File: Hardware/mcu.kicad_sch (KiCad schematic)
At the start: 10 parts, among them Q1 BSS138DW-7-F, U6 AS7341-DLGT

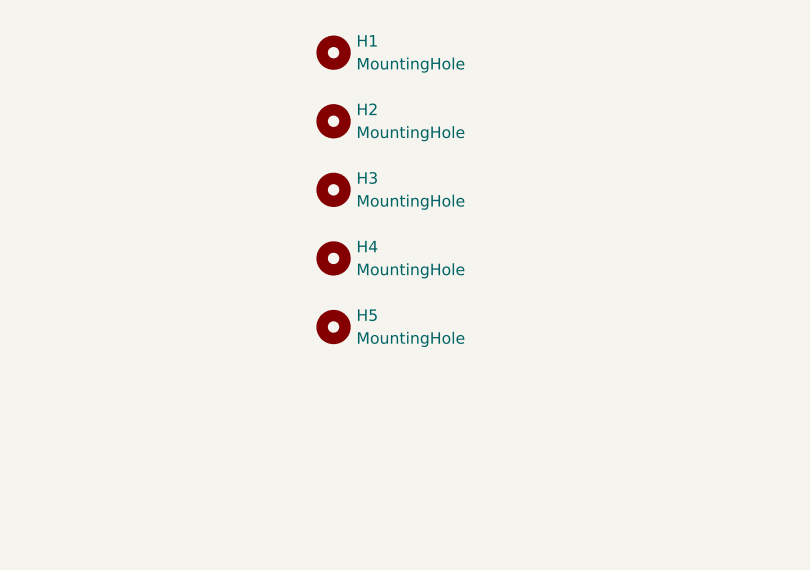
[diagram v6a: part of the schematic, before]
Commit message: initial branch commit with rought layout changes
Signed-off-by: Lawrence Kincheloe <lawrence.kincheloe@mavericktechok.com>
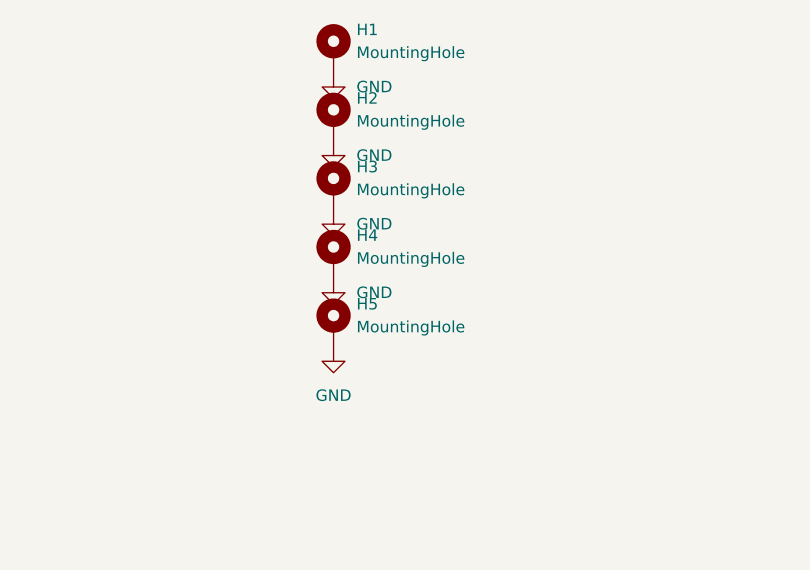
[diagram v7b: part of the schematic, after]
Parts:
- H1, H2, H3, H4, H5: symbol Mechanical:MountingHole -> Mechanical:MountingHole_Pad
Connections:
- net GND: now also H1.1, H2.1, H3.1, H4.1, H5.1
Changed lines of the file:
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@@
     (pin "2")
   )
-  (symbol (lib_id "Mechanical:MountingHole") (at 182.88 39.37 0) (unit 1)
-    (in_bom yes) (on_board yes) (fields_autoplaced)
-    (property "Reference" "H2" (id 0) (at 185.42 38.0999 0)
-      (effects (font (size 1.27 1.27)) (justify left))
-    )
-    (property "Value" "MountingHole" (id 1) (at 185.42 40.6399 0)
+  (symbol (lib_id "power:GND") (at 182.88 64.77 0) (unit 1)
+    (in_bom yes) (on_board yes) (fields_autoplaced)
+    (property "Reference" "#PWR0134" (id 0) (at 182.88 71.12 0)
+      (effects (font (size 1.27 1.27)) hide)
+    )
+    (property "Value" "GND" (id 1) (at 182.88 69.85 0))
+    (property "Footprint" "" (id 2) (at 182.88 64.77 0)
+      (effects (font (size 1.27 1.27)) hide)
+    )
+    (property "Datasheet" "" (id 3) (at 182.88 64.77 0)
+      (effects (font (size 1.27 1.27)) hide)
+    )
+    (pin "1")
+  )
+  (symbol (lib_id "power:GND") (at 182.88 34.29 0) (unit 1)
+    (in_bom yes) (on_board yes) (fields_autoplaced)
+    (property "Reference" "#PWR0112" (id 0) (at 182.88 40.64 0)
+      (effects (font (size 1.27 1.27)) hide)
+    )
+    (property "Value" "GND" (id 1) (at 185.42 35.5599 0)
+      (effects (font (size 1.27 1.27)) (justify left))
+    )
+    (property "Footprint" "" (id 2) (at 182.88 34.29 0)
+      (effects (font (size 1.27 1.27)) hide)
+    )
+    (property "Datasheet" "" (id 3) (at 182.88 34.29 0)
+      (effects (font (size 1.27 1.27)) hide)
+    )
+    (pin "1")
+  )
+  (symbol (lib_id "Mechanical:MountingHole_Pad") (at 182.88 39.37 0) (unit 1)
+    (in_bom yes) (on_board yes) (fields_autoplaced)
+    (property "Reference" "H2" (id 0) (at 185.42 36.8299 0)
+      (effects (font (size 1.27 1.27)) (justify left))
+    )
+    (property "Value" "MountingHole" (id 1) (at 185.42 39.3699 0)
       (effects (font (size 1.27 1.27)) (justify left))
     )
@@
       (effects (font (size 1.27 1.27)) hide)
     )
+    (pin "1")
   )
   (symbol (lib_id "Everlight-EAHC2835WD6:EAHC2835WD6") (at 180.34 102.87 270) (unit 1)
@@
     (pin "2")
   )
-  (symbol (lib_id "Mechanical:MountingHole") (at 182.88 62.23 0) (unit 1)
-    (in_bom yes) (on_board yes) (fields_autoplaced)
-    (property "Reference" "H5" (id 0) (at 185.42 60.9599 0)
-      (effects (font (size 1.27 1.27)) (justify left))
-    )
-    (property "Value" "MountingHole" (id 1) (at 185.42 63.4999 0)
+  (symbol (lib_id "Mechanical:MountingHole_Pad") (at 182.88 62.23 0) (unit 1)
+    (in_bom yes) (on_board yes) (fields_autoplaced)
+    (property "Reference" "H5" (id 0) (at 185.42 59.6899 0)
+      (effects (font (size 1.27 1.27)) (justify left))
+    )
+    (property "Value" "MountingHole" (id 1) (at 185.42 62.2299 0)
       (effects (font (size 1.27 1.27)) (justify left))
     )
@@
       (effects (font (size 1.27 1.27)) hide)
     )
+    (pin "1")
   )
   (symbol (lib_id "power:+3.3V") (at 180.34 102.87 0) (unit 1)
@@
     (pin "1")
   )
-  (symbol (lib_id "Mechanical:MountingHole") (at 182.88 46.99 0) (unit 1)
-    (in_bom yes) (on_board yes) (fields_autoplaced)
-    (property "Reference" "H3" (id 0) (at 185.42 45.7199 0)
-      (effects (font (size 1.27 1.27)) (justify left))
-    )
-    (property "Value" "MountingHole" (id 1) (at 185.42 48.2599 0)
+  (symbol (lib_id "power:GND") (at 182.88 49.53 0) (unit 1)
+    (in_bom yes) (on_board yes) (fields_autoplaced)
+    (property "Reference" "#PWR0135" (id 0) (at 182.88 55.88 0)
+      (effects (font (size 1.27 1.27)) hide)
+    )
+    (property "Value" "GND" (id 1) (at 185.42 50.7999 0)
+      (effects (font (size 1.27 1.27)) (justify left))
+    )
+    (property "Footprint" "" (id 2) (at 182.88 49.53 0)
+      (effects (font (size 1.27 1.27)) hide)
+    )
+    (property "Datasheet" "" (id 3) (at 182.88 49.53 0)
+      (effects (font (size 1.27 1.27)) hide)
+    )
+    (pin "1")
+  )
+  (symbol (lib_id "Mechanical:MountingHole_Pad") (at 182.88 46.99 0) (unit 1)
+    (in_bom yes) (on_board yes) (fields_autoplaced)
+    (property "Reference" "H3" (id 0) (at 185.42 44.4499 0)
+      (effects (font (size 1.27 1.27)) (justify left))
+    )
+    (property "Value" "MountingHole" (id 1) (at 185.42 46.9899 0)
       (effects (font (size 1.27 1.27)) (justify left))
     )
@@
       (effects (font (size 1.27 1.27)) hide)
     )
+    (pin "1")
   )
   (symbol (lib_id "Diodes_Inc._-_BSS138DW-7-F:BSS138DW-7-F") (at 91.44 100.33 270) (unit 1)
@@
     (pin "4")
     (pin "5")
-    (pin "1")
-    (pin "2")
-    (pin "6")
   )
   (symbol (lib_id "power:GND") (at 257.81 132.08 0) (unit 1)
@@
     (pin "2")
   )
-  (symbol (lib_id "Mechanical:MountingHole") (at 182.88 54.61 0) (unit 1)
-    (in_bom yes) (on_board yes) (fields_autoplaced)
-    (property "Reference" "H4" (id 0) (at 185.42 53.3399 0)
-      (effects (font (size 1.27 1.27)) (justify left))
-    )
-    (property "Value" "MountingHole" (id 1) (at 185.42 55.8799 0)
+  (symbol (lib_id "Mechanical:MountingHole_Pad") (at 182.88 54.61 0) (unit 1)
+    (in_bom yes) (on_board yes) (fields_autoplaced)
+    (property "Reference" "H4" (id 0) (at 185.42 52.0699 0)
+      (effects (font (size 1.27 1.27)) (justify left))
+    )
+    (property "Value" "MountingHole" (id 1) (at 185.42 54.6099 0)
       (effects (font (size 1.27 1.27)) (justify left))
     )
@@
       (effects (font (size 1.27 1.27)) hide)
     )
+    (pin "1")
   )
   (symbol (lib_id "AS7341-DLGT:AS7341-DLGT") (at 236.22 119.38 0) (unit 1)
@@
     (pin "8")
   )
-  (symbol (lib_id "Mechanical:MountingHole") (at 182.88 31.75 0) (unit 1)
-    (in_bom yes) (on_board yes) (fields_autoplaced)
-    (property "Reference" "H1" (id 0) (at 185.42 30.4799 0)
-      (effects (font (size 1.27 1.27)) (justify left))
-    )
-    (property "Value" "MountingHole" (id 1) (at 185.42 33.0199 0)
+  (symbol (lib_id "power:GND") (at 182.88 57.15 0) (unit 1)
+    (in_bom yes) (on_board yes) (fields_autoplaced)
+    (property "Reference" "#PWR0133" (id 0) (at 182.88 63.5 0)
+      (effects (font (size 1.27 1.27)) hide)
+    )
+    (property "Value" "GND" (id 1) (at 185.42 58.4199 0)
+      (effects (font (size 1.27 1.27)) (justify left))
+    )
+    (property "Footprint" "" (id 2) (at 182.88 57.15 0)
+      (effects (font (size 1.27 1.27)) hide)
+    )
+    (property "Datasheet" "" (id 3) (at 182.88 57.15 0)
+      (effects (font (size 1.27 1.27)) hide)
+    )
+    (pin "1")
+  )
+  (symbol (lib_id "Mechanical:MountingHole_Pad") (at 182.88 31.75 0) (unit 1)
+    (in_bom yes) (on_board yes) (fields_autoplaced)
+    (property "Reference" "H1" (id 0) (at 185.42 29.2099 0)
+      (effects (font (size 1.27 1.27)) (justify left))
+    )
+    (property "Value" "MountingHole" (id 1) (at 185.42 31.7499 0)
       (effects (font (size 1.27 1.27)) (justify left))
     )
@@
       (effects (font (size 1.27 1.27)) hide)
     )
+    (pin "1")
   )
   (symbol (lib_id "power:+1V8") (at 257.81 106.68 0) (unit 1)
@@
     )
     (property "Datasheet" "" (id 3) (at 68.58 92.71 0)
+      (effects (font (size 1.27 1.27)) hide)
+    )
+    (pin "1")
+  )
+  (symbol (lib_id "power:GND") (at 182.88 41.91 0) (unit 1)
+    (in_bom yes) (on_board yes) (fields_autoplaced)
+    (property "Reference" "#PWR0108" (id 0) (at 182.88 48.26 0)
+      (effects (font (size 1.27 1.27)) hide)
+    )
+    (property "Value" "GND" (id 1) (at 185.42 43.1799 0)
+      (effects (font (size 1.27 1.27)) (justify left))
+    )
+    (property "Footprint" "" (id 2) (at 182.88 41.91 0)
+      (effects (font (size 1.27 1.27)) hide)
+    )
+    (property "Datasheet" "" (id 3) (at 182.88 41.91 0)
       (effects (font (size 1.27 1.27)) hide)
     )
@@
       (effects (font (size 1.27 1.27)) (justify left) hide)
     )
-    (pin "3")
-    (pin "4")
-    (pin "5")
     (pin "1")
     (pin "2")
